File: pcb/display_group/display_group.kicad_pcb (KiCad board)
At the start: 2 copper layers, 79.6 x 24.8 mm, 10 parts, among them J1 L, J16 R, J17 L, J18 R, J2 R, J3 SELECT, J4 SEGMENTS, J5 L, J6 R, J7 L

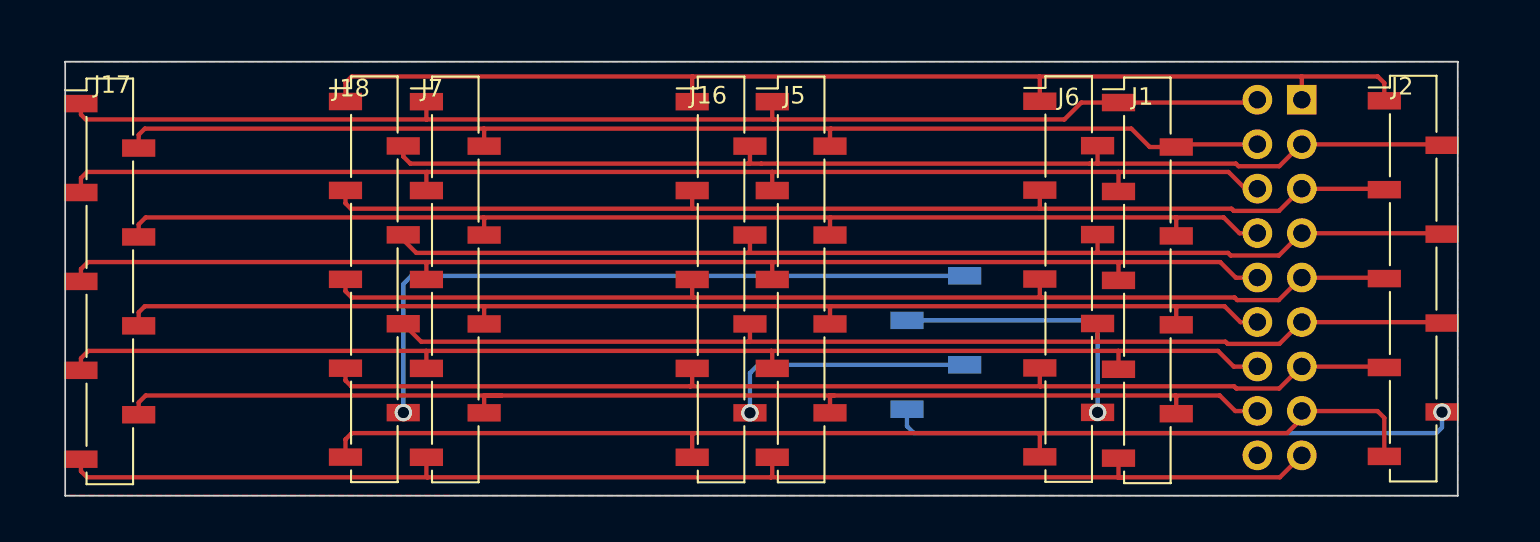
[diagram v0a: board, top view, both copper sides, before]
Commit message: cleaned up, reworked and (so far) finalized the display-group board
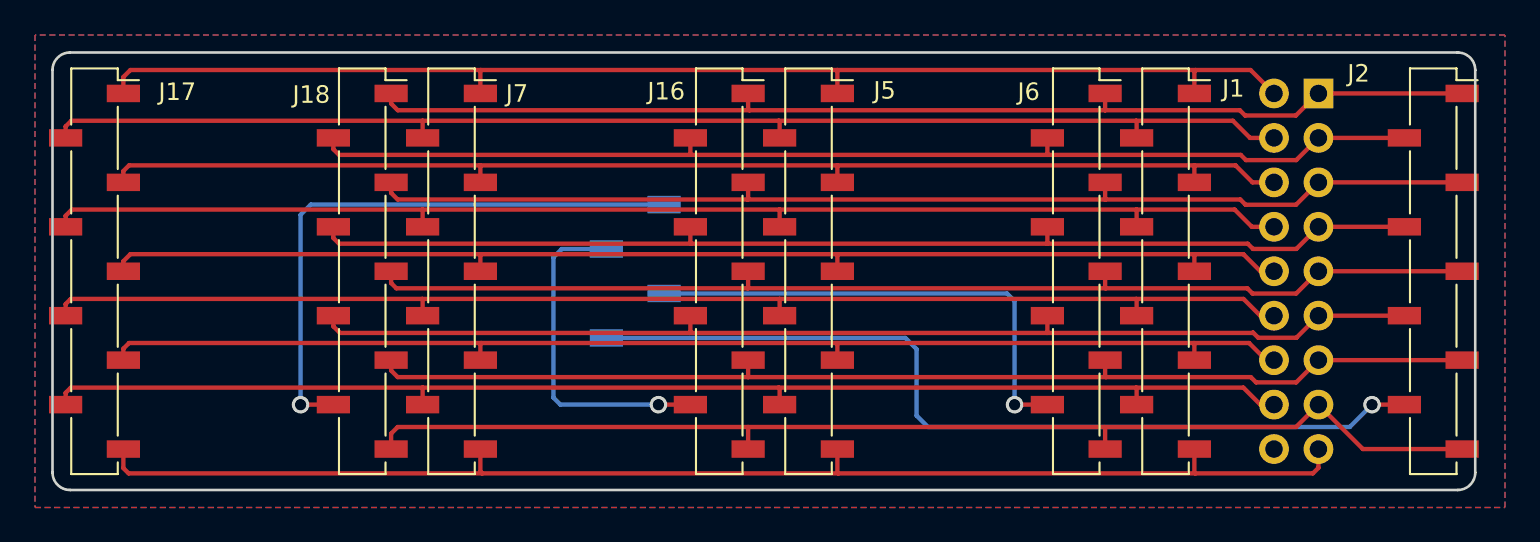
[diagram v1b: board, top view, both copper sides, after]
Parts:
- J1, J16, J17, J18, J2, J5, J6, J7: footprint Connector_PinSocket_2.54mm:PinSocket_1x09_P2.54mm_Vertical_SMD_Pin1Left -> Connector_PinSocket_2.54mm:PinSocket_1x09_P2.54mm_Vertical_SMD_Pin1Right
- moved J3 17.7 mm to (111.3, 140.5)
- moved J2 1.22 mm to (156.9, 140.5)
- moved J1 1.16 mm to (141.6, 140.5)
- moved J17 1.05 mm to (80.4, 140.5)
- moved J4 1.02 mm to (150.3, 130.3)
- moved J18 0.83 mm to (95.7, 140.5)
- moved J5 0.63 mm to (121.2, 140.5)
- moved J6 0.62 mm to (136.5, 140.5)
- moved J7 0.52 mm to (100.8, 140.5)
- moved J16 0.48 mm to (116.1, 140.5)
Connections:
- net DB_A renamed A
- net DB_B renamed B
- net DB_C renamed C
- net DB_D renamed D
- net DB_DISPLAY1_GND renamed DISPLAY1_GND
- net DB_DISPLAY2_GND renamed DISPLAY2_GND
- net DB_DISPLAY3_GND renamed DISPLAY3_GND
- net DB_DISPLAY4_GND renamed DISPLAY4_GND
- net DB_DP renamed DP
- net DB_E renamed E
- net DB_F renamed F
- net DB_G renamed G
- net DB_H renamed H
- net DB_I renamed I
- net DB_J renamed J
- net DB_K renamed K
- net DB_L renamed L
- net DB_M renamed M
- net DB_N renamed N
- net DB_O renamed O
- net DB_P renamed P
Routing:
- net DISPLAY4_GND: track 32.7 -> 50.5 mm
- net DISPLAY3_GND: track 14.7 -> 28.0 mm
- net J: track 67.3 -> 73.2 mm
- net DISPLAY1_GND: track 39.6 -> 33.7 mm
- net H: track 68.2 -> 73.2 mm
- net N: track 68.3 -> 73.1 mm
- net G: track 69.4 -> 73.2 mm
- net DISPLAY2_GND: track 15.9 -> 19.2 mm
- net D: track 62.5 -> 64.6 mm
- net I: track 71.8 -> 69.9 mm
- net L: track 62.7 -> 64.6 mm
- net K: track 62.8 -> 64.6 mm
- net P: track 71.5 -> 69.8 mm
- net M: track 63.0 -> 64.6 mm
- net C: track 62.9 -> 64.6 mm
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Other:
- board size 79.6 x 24.8 mm -> 81.3 x 25 mm
